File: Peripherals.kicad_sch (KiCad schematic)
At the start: 13 parts, among them J2 TF-102-15, J3 Screw_Terminal_01x12, J4 Screw_Terminal_01x02, J5 Conn_01x05, J6 Conn_01x04, U13 74LVC1G04, U2 DRV8210DRLR

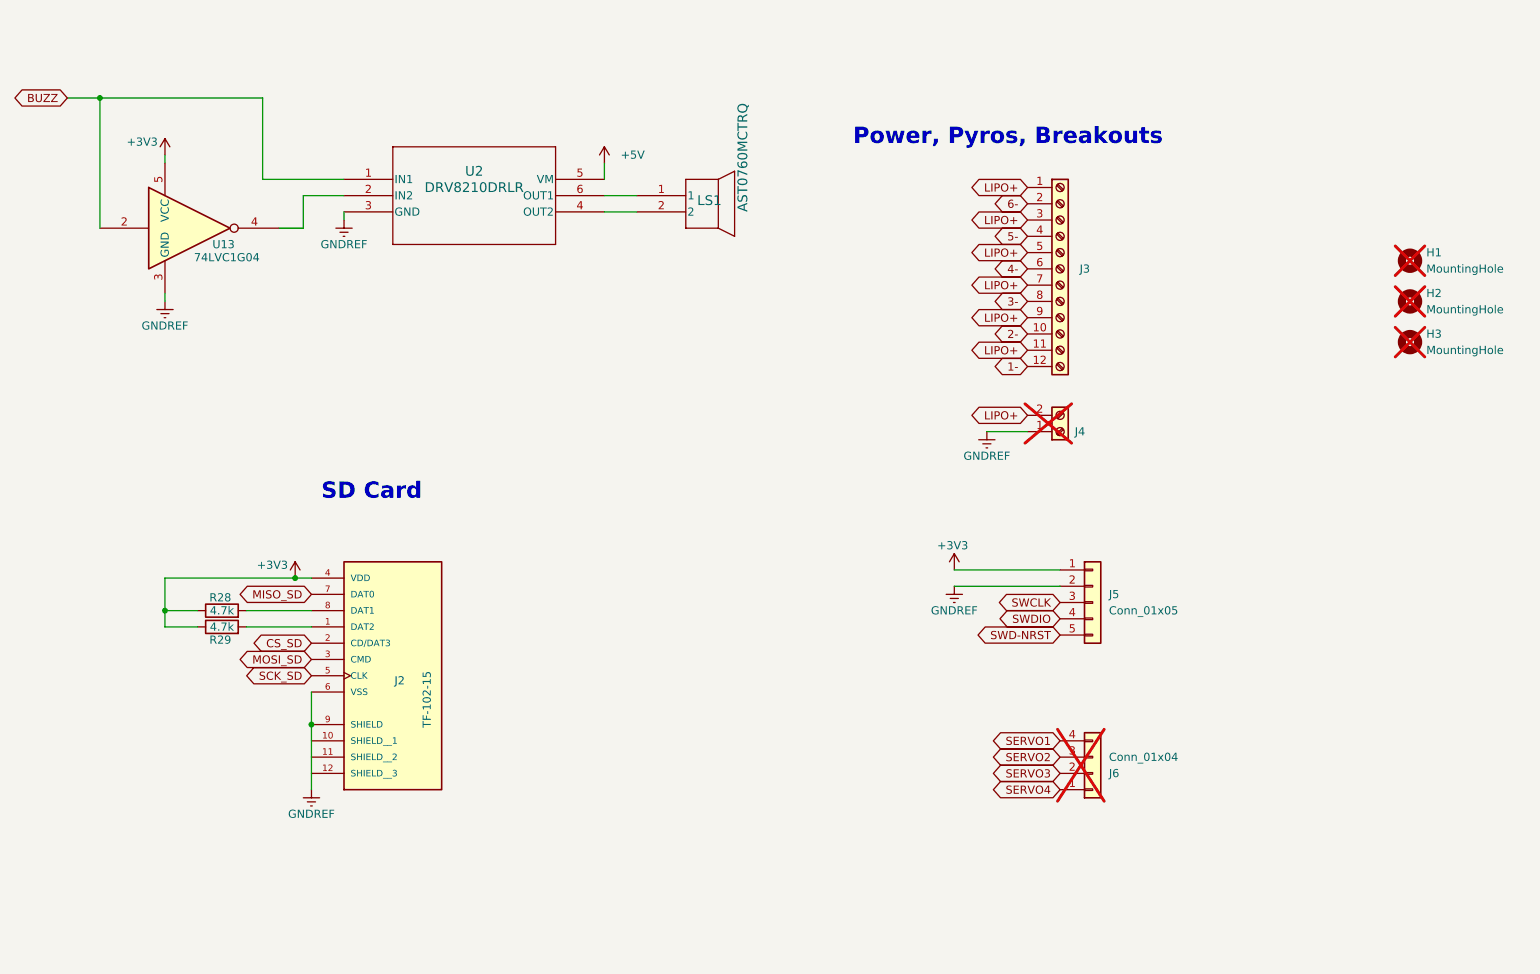
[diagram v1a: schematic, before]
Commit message: updated power delivery and component choices. v4 now ready
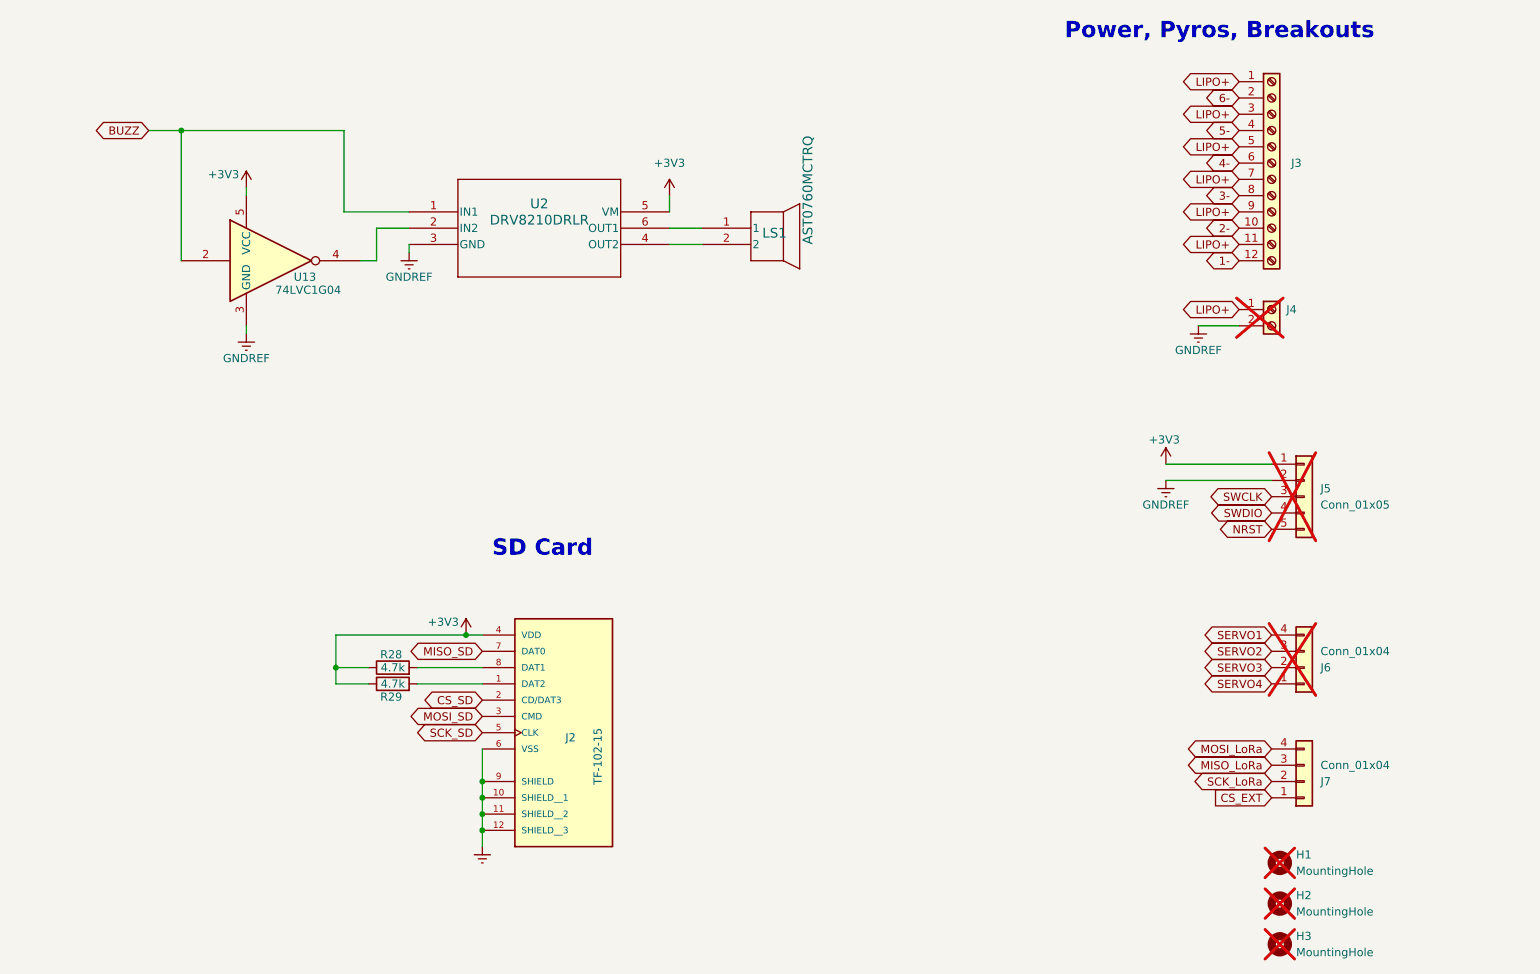
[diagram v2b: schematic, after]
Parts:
- added J7: Conn_01x04, Connector_PinHeader_2.54mm:PinHeader_1x04_P2.54mm_Vertical, symbol Connector_Generic:Conn_01x04
- J4: footprint Connector_PinHeader_2.54mm:PinHeader_1x02_P2.54mm_Vertical -> Connector_Wire:SolderWire-0.75sqmm_1x02_P7mm_D1.25mm_OD3.5mm
- J5: now not fitted
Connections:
- net +5V is gone; now on net +3V3: U2.5 (VM)
- net GNDREF: now also J2.10 (SHIELD__1), J2.11 (SHIELD__2), J2.12 (SHIELD__3), J4.2 (Pin_2); no longer J4.1 (Pin_1)
- net LIPO+: now also J4.1 (Pin_1); no longer J4.2 (Pin_2)
- net SWD-NRST renamed NRST
- new net CS_EXT: J7.1 (Pin_1)
- new net MISO_LoRa: J7.3 (Pin_3)
- new net MOSI_LoRa: J7.4 (Pin_4)
- new net SCK_LoRa: J7.2 (Pin_2)
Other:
- moved on the sheet: H1, H2, H3, J2, J3, J4, J6, LS1, R28, R29, U13, U2
